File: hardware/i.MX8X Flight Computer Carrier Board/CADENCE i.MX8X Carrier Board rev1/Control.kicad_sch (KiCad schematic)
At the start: 9 parts, among them SW1 SW_DIP_x04, SW2 KMR221GLFS, SW3 SW_DIP_x01

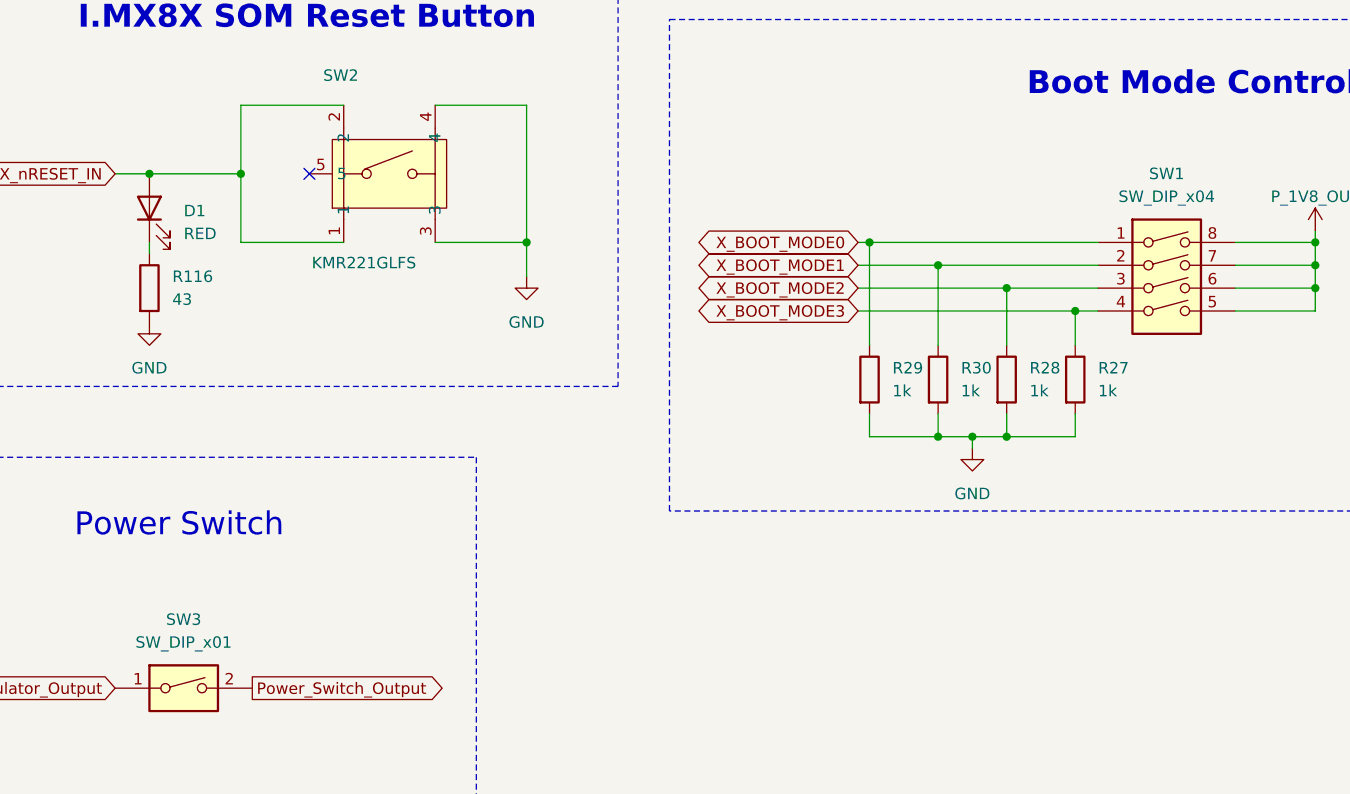
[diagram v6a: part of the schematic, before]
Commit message: added termination resistors for ebyte spi bus & fixed some erc issues
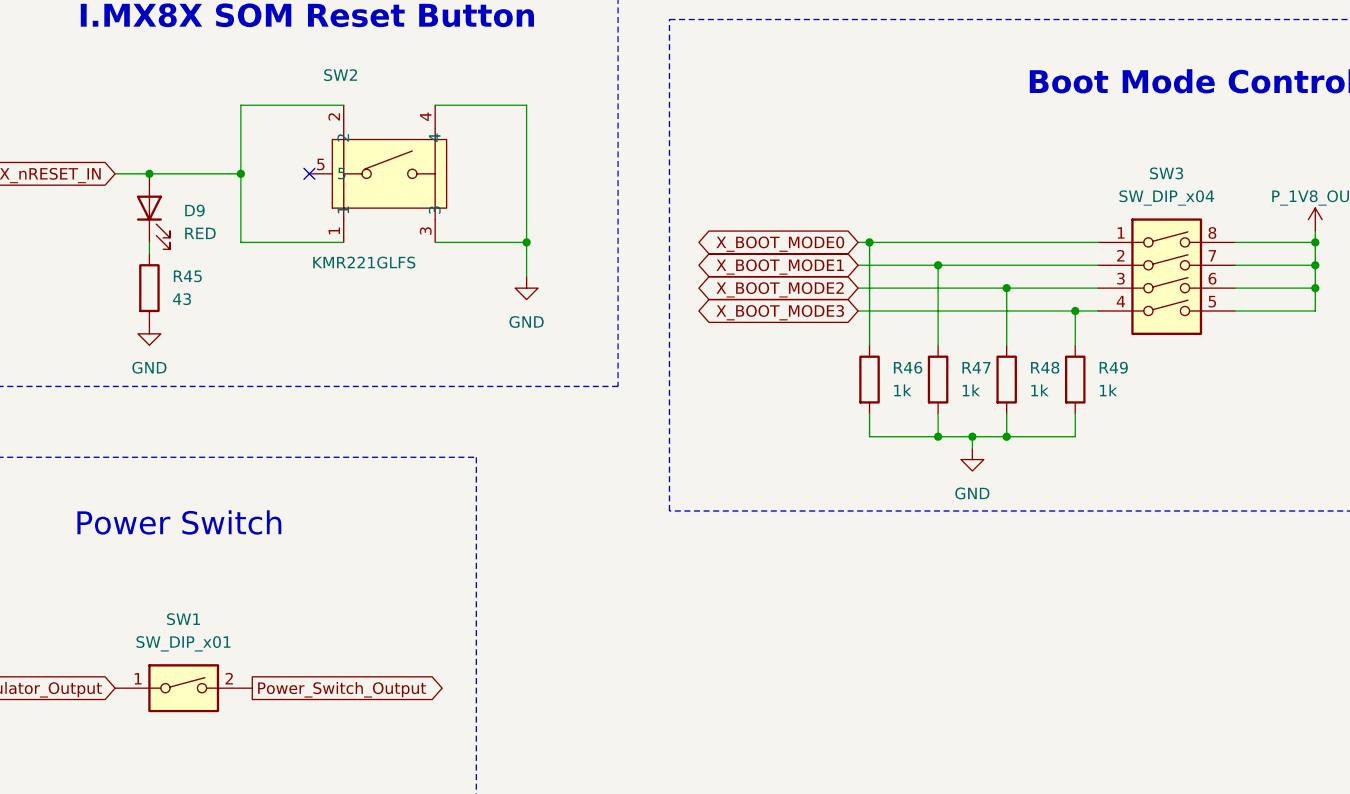
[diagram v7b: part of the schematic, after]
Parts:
- renumbered D1 to D9, R116 to R45, R29 to R46, R30 to R47, R28 to R48, R27 to R49, SW3 to SW1, SW1 to SW3
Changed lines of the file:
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@@
 		(dnp no)
 		(fields_autoplaced yes)
-		(property "Reference" "SW1"
+		(property "Reference" "SW3"
 			(at 161.29 41.91 0)
 			(effects
@@
 			(project "CADENCE i.MX8X Carrier Board rev1"
 				(path "/de284495-d382-47cb-b528-76e440980d40/089c604b-0863-4822-93dd-cc06ae04e525"
-					(reference "SW1")
+					(reference "SW3")
 					(unit 1)
 				)
@@
 		(dnp no)
 		(fields_autoplaced yes)
-		(property "Reference" "D1"
+		(property "Reference" "D9"
 			(at 52.07 46.0374 90)
 			(effects
@@
 			(project ""
 				(path "/de284495-d382-47cb-b528-76e440980d40/089c604b-0863-4822-93dd-cc06ae04e525"
-					(reference "D1")
+					(reference "D9")
 					(unit 1)
 				)
@@
 		(dnp no)
 		(fields_autoplaced yes)
-		(property "Reference" "#PWR0111"
+		(property "Reference" "#PWR048"
 			(at 90.17 59.69 0)
 			(effects
@@
 			(project ""
 				(path "/de284495-d382-47cb-b528-76e440980d40/089c604b-0863-4822-93dd-cc06ae04e525"
-					(reference "#PWR0111")
+					(reference "#PWR048")
 					(unit 1)
 				)
@@
 		(dnp no)
 		(fields_autoplaced yes)
-		(property "Reference" "#PWR016"
+		(property "Reference" "#PWR049"
 			(at 139.7 78.74 0)
 			(effects
@@
 			(project "CADENCE i.MX8X Carrier Board rev1"
 				(path "/de284495-d382-47cb-b528-76e440980d40/089c604b-0863-4822-93dd-cc06ae04e525"
-					(reference "#PWR016")
+					(reference "#PWR049")
 					(unit 1)
 				)
@@
 		(dnp no)
 		(fields_autoplaced yes)
-		(property "Reference" "R28"
+		(property "Reference" "R48"
 			(at 146.05 63.4999 0)
 			(effects
@@
 			(project "CADENCE i.MX8X Carrier Board rev1"
 				(path "/de284495-d382-47cb-b528-76e440980d40/089c604b-0863-4822-93dd-cc06ae04e525"
-					(reference "R28")
+					(reference "R48")
 					(unit 1)
 				)
@@
 		(dnp no)
 		(fields_autoplaced yes)
-		(property "Reference" "SW3"
+		(property "Reference" "SW1"
 			(at 52.07 91.44 0)
 			(effects
@@
 			(project ""
 				(path "/de284495-d382-47cb-b528-76e440980d40/089c604b-0863-4822-93dd-cc06ae04e525"
-					(reference "SW3")
+					(reference "SW1")
 					(unit 1)
 				)
@@
 		(dnp no)
 		(fields_autoplaced yes)
-		(property "Reference" "R30"
+		(property "Reference" "R47"
 			(at 138.43 63.4999 0)
 			(effects
@@
 			(project "CADENCE i.MX8X Carrier Board rev1"
 				(path "/de284495-d382-47cb-b528-76e440980d40/089c604b-0863-4822-93dd-cc06ae04e525"
-					(reference "R30")
+					(reference "R47")
 					(unit 1)
 				)
@@
 		(dnp no)
 		(fields_autoplaced yes)
-		(property "Reference" "R27"
+		(property "Reference" "R49"
 			(at 153.67 63.4999 0)
 			(effects
@@
 			(project ""
 				(path "/de284495-d382-47cb-b528-76e440980d40/089c604b-0863-4822-93dd-cc06ae04e525"
-					(reference "R27")
+					(reference "R49")
 					(unit 1)
 				)
@@
 		(dnp no)
 		(fields_autoplaced yes)
-		(property "Reference" "#PWR0180"
+		(property "Reference" "#PWR047"
 			(at 48.26 64.77 0)
 			(effects
@@
 			(project "CADENCE i.MX8X Carrier Board rev1"
 				(path "/de284495-d382-47cb-b528-76e440980d40/089c604b-0863-4822-93dd-cc06ae04e525"
-					(reference "#PWR0180")
+					(reference "#PWR047")
 					(unit 1)
 				)
@@
 		(on_board yes)
 		(dnp no)
-		(property "Reference" "#PWR0112"
+		(property "Reference" "#PWR050"
 			(at 177.8 52.07 0)
 			(effects
@@
 			(project "CADENCE i.MX8X Carrier Board rev1"
 				(path "/de284495-d382-47cb-b528-76e440980d40/089c604b-0863-4822-93dd-cc06ae04e525"
-					(reference "#PWR0112")
+					(reference "#PWR050")
 					(unit 1)
 				)
@@
 		(dnp no)
 		(fields_autoplaced yes)
-		(property "Reference" "R29"
+		(property "Reference" "R46"
 			(at 130.81 63.4999 0)
 			(effects
@@
 			(project "CADENCE i.MX8X Carrier Board rev1"
 				(path "/de284495-d382-47cb-b528-76e440980d40/089c604b-0863-4822-93dd-cc06ae04e525"
-					(reference "R29")
+					(reference "R46")
 					(unit 1)
 				)
@@
 		(dnp no)
 		(fields_autoplaced yes)
-		(property "Reference" "R116"
+		(property "Reference" "R45"
 			(at 50.8 53.3399 0)
 			(effects
@@
 			(project "CADENCE i.MX8X Carrier Board rev1"
 				(path "/de284495-d382-47cb-b528-76e440980d40/089c604b-0863-4822-93dd-cc06ae04e525"
-					(reference "R116")
-					(unit 1)
-				)
+					(reference "R45")
+					(unit 1)
+				)

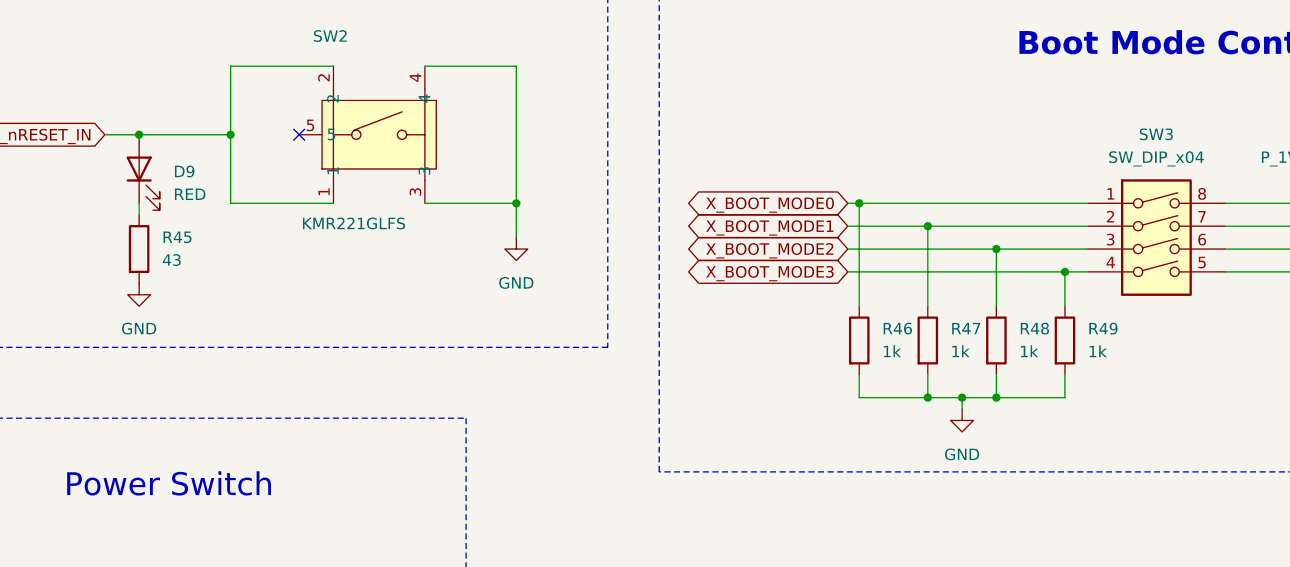
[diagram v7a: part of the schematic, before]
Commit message: Added pin definitions page
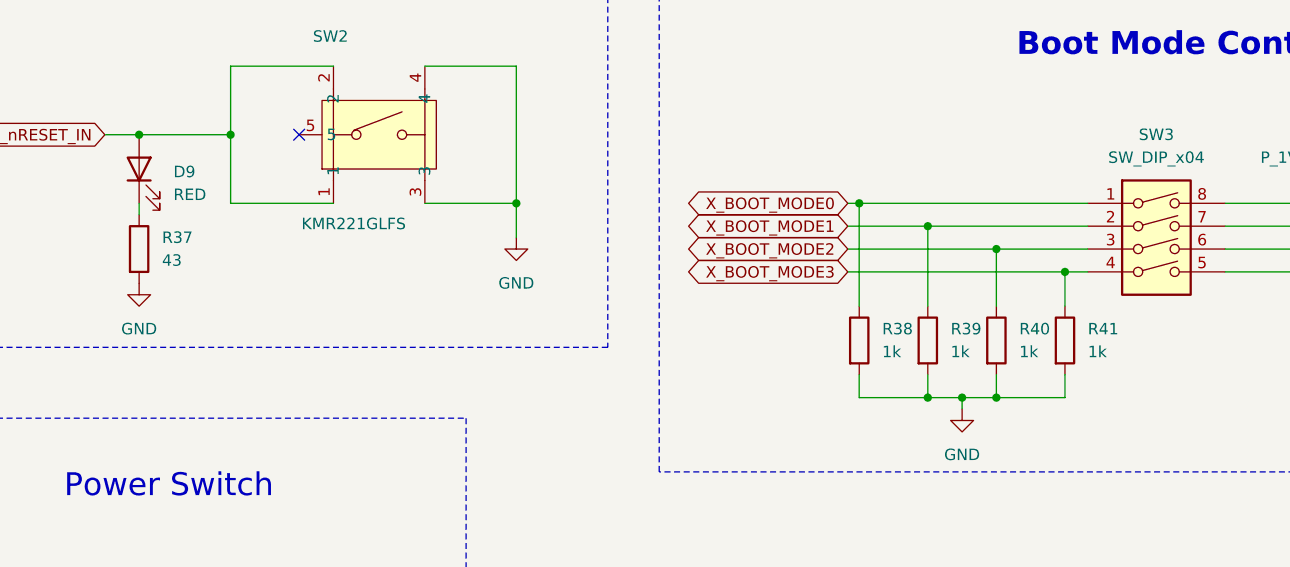
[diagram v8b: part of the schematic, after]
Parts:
- renumbered R45 to R37, R46 to R38, R47 to R39, R48 to R40, R49 to R41
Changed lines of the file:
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@@
 		(dnp no)
 		(fields_autoplaced yes)
-		(property "Reference" "#PWR048"
+		(property "Reference" "#PWR049"
 			(at 90.17 59.69 0)
 			(effects
@@
 			(project ""
 				(path "/de284495-d382-47cb-b528-76e440980d40/089c604b-0863-4822-93dd-cc06ae04e525"
-					(reference "#PWR048")
+					(reference "#PWR049")
 					(unit 1)
 				)
@@
 		(dnp no)
 		(fields_autoplaced yes)
-		(property "Reference" "#PWR049"
+		(property "Reference" "#PWR050"
 			(at 139.7 78.74 0)
 			(effects
@@
 			(project "CADENCE i.MX8X Carrier Board rev1"
 				(path "/de284495-d382-47cb-b528-76e440980d40/089c604b-0863-4822-93dd-cc06ae04e525"
-					(reference "#PWR049")
+					(reference "#PWR050")
 					(unit 1)
 				)
@@
 		(dnp no)
 		(fields_autoplaced yes)
-		(property "Reference" "R48"
+		(property "Reference" "R40"
 			(at 146.05 63.4999 0)
 			(effects
@@
 			(project "CADENCE i.MX8X Carrier Board rev1"
 				(path "/de284495-d382-47cb-b528-76e440980d40/089c604b-0863-4822-93dd-cc06ae04e525"
-					(reference "R48")
+					(reference "R40")
 					(unit 1)
 				)
@@
 		(dnp no)
 		(fields_autoplaced yes)
-		(property "Reference" "R47"
+		(property "Reference" "R39"
 			(at 138.43 63.4999 0)
 			(effects
@@
 			(project "CADENCE i.MX8X Carrier Board rev1"
 				(path "/de284495-d382-47cb-b528-76e440980d40/089c604b-0863-4822-93dd-cc06ae04e525"
-					(reference "R47")
+					(reference "R39")
 					(unit 1)
 				)
@@
 		(dnp no)
 		(fields_autoplaced yes)
-		(property "Reference" "R49"
+		(property "Reference" "R41"
 			(at 153.67 63.4999 0)
 			(effects
@@
 			(project ""
 				(path "/de284495-d382-47cb-b528-76e440980d40/089c604b-0863-4822-93dd-cc06ae04e525"
-					(reference "R49")
+					(reference "R41")
 					(unit 1)
 				)
@@
 		(dnp no)
 		(fields_autoplaced yes)
-		(property "Reference" "#PWR047"
+		(property "Reference" "#PWR048"
 			(at 48.26 64.77 0)
 			(effects
@@
 			(project "CADENCE i.MX8X Carrier Board rev1"
 				(path "/de284495-d382-47cb-b528-76e440980d40/089c604b-0863-4822-93dd-cc06ae04e525"
-					(reference "#PWR047")
+					(reference "#PWR048")
 					(unit 1)
 				)
@@
 		(on_board yes)
 		(dnp no)
-		(property "Reference" "#PWR050"
+		(property "Reference" "#PWR051"
 			(at 177.8 52.07 0)
 			(effects
@@
 			(project "CADENCE i.MX8X Carrier Board rev1"
 				(path "/de284495-d382-47cb-b528-76e440980d40/089c604b-0863-4822-93dd-cc06ae04e525"
-					(reference "#PWR050")
+					(reference "#PWR051")
 					(unit 1)
 				)
@@
 		(dnp no)
 		(fields_autoplaced yes)
-		(property "Reference" "R46"
+		(property "Reference" "R38"
 			(at 130.81 63.4999 0)
 			(effects
@@
 			(project "CADENCE i.MX8X Carrier Board rev1"
 				(path "/de284495-d382-47cb-b528-76e440980d40/089c604b-0863-4822-93dd-cc06ae04e525"
-					(reference "R46")
+					(reference "R38")
 					(unit 1)
 				)
@@
 		(dnp no)
 		(fields_autoplaced yes)
-		(property "Reference" "R45"
+		(property "Reference" "R37"
 			(at 50.8 53.3399 0)
 			(effects
@@
 			(project "CADENCE i.MX8X Carrier Board rev1"
 				(path "/de284495-d382-47cb-b528-76e440980d40/089c604b-0863-4822-93dd-cc06ae04e525"
-					(reference "R45")
-					(unit 1)
-				)
+					(reference "R37")
+					(unit 1)
+				)
